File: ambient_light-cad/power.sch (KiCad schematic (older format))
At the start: 27 parts

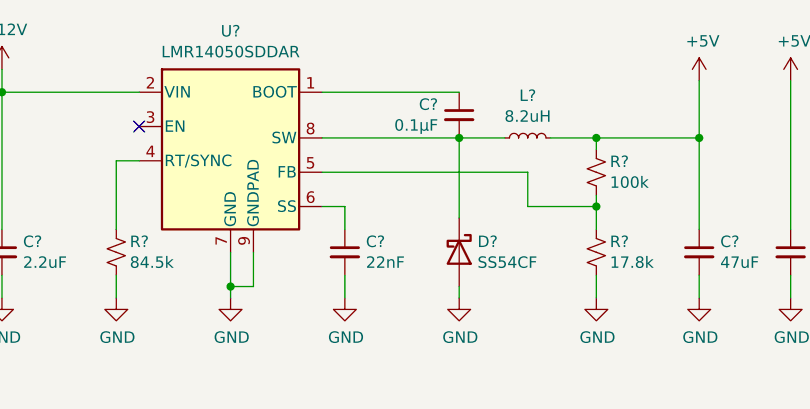
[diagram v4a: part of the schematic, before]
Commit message: [Updated] Symbol field for PCB layout
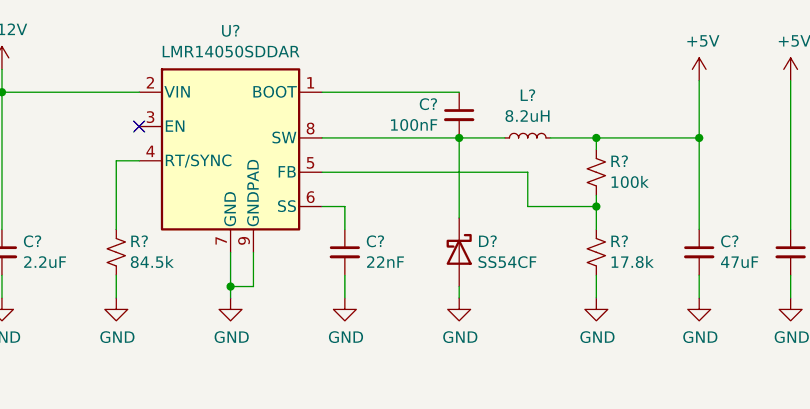
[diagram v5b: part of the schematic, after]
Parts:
- C? (x4): footprint (none) -> Capacitor_SMD:C_0603_1608Metric_Pad1.08x0.95mm_HandSolder
- C? (x4): footprint (none) -> Capacitor_Tantalum_SMD:CP_EIA-3216-18_Kemet-A_Pad1.58x1.35mm_HandSolder
- C?: value 0.1μF -> 100nF; footprint (none) -> Capacitor_SMD:C_0603_1608Metric_Pad1.08x0.95mm_HandSolder
- D?: footprint (none) -> Diode_SMD:D_SMC
- J?: footprint (none) -> Connector_BarrelJack:BarrelJack_Horizontal
- L?: footprint (none) -> Inductor_SMD:L_12x12mm_H8mm
- Q?: footprint (none) -> Package_TO_SOT_SMD:SOT-23
- R? (x5): footprint (none) -> Resistor_SMD:R_0603_1608Metric_Pad0.98x0.95mm_HandSolder
- TP? (x6): footprint (none) -> TestPoint:TestPoint_Pad_D2.0mm
- U?: footprint Package_SO:TI_SO-PowerPAD-8_ThermalVias -> Package_SO:TI_SO-PowerPAD-8
- U? (x2): footprint (none) -> Package_SO:SOIC-8_3.9x4.9mm_P1.27mm
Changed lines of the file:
@@
 F 0 "J?" H 1407 2217 50  0000 C CNN
 F 1 "Barrel_Jack_Switch" H 1407 2126 50  0000 C CNN
-F 2 "" H 1400 1860 50  0001 C CNN
+F 2 "Connector_BarrelJack:BarrelJack_Horizontal" H 1400 1860 50  0001 C CNN
 F 3 "~" H 1400 1860 50  0001 C CNN
 	1    1350 1900
@@
 F 0 "C?" H 3642 2246 50  0000 L CNN
 F 1 "2.2uF" H 3642 2155 50  0000 L CNN
-F 2 "" H 3550 2200 50  0001 C CNN
+F 2 "Capacitor_SMD:C_0603_1608Metric_Pad1.08x0.95mm_HandSolder" H 3550 2200 50  0001 C CNN
 F 3 "~" H 3550 2200 50  0001 C CNN
 	1    3550 2200
@@
 F 0 "R?" H 4109 2246 50  0000 L CNN
 F 1 "84.5k" H 4109 2155 50  0000 L CNN
-F 2 "" H 4050 2200 50  0001 C CNN
+F 2 "Resistor_SMD:R_0603_1608Metric_Pad0.98x0.95mm_HandSolder" H 4050 2200 50  0001 C CNN
 F 3 "~" H 4050 2200 50  0001 C CNN
 	1    4050 2200
@@
 F 0 "L?" V 6035 1700 50  0000 C CNN
 F 1 "8.2uH" V 5944 1700 50  0000 C CNN
-F 2 "" H 5850 1700 50  0001 C CNN
+F 2 "Inductor_SMD:L_12x12mm_H8mm" H 5850 1700 50  0001 C CNN
 F 3 "~" H 5850 1700 50  0001 C CNN
 	1    5850 1700
@@
 F 0 "C?" H 6692 2246 50  0000 L CNN
 F 1 "47uF" H 6692 2155 50  0000 L CNN
-F 2 "" H 6600 2200 50  0001 C CNN
+F 2 "Capacitor_Tantalum_SMD:CP_EIA-3216-18_Kemet-A_Pad1.58x1.35mm_HandSolder" H 6600 2200 50  0001 C CNN
 F 3 "~" H 6600 2200 50  0001 C CNN
 	1    6600 2200
@@
 F 0 "R?" H 6209 2246 50  0000 L CNN
 F 1 "17.8k" H 6209 2155 50  0000 L CNN
-F 2 "" H 6150 2200 50  0001 C CNN
+F 2 "Resistor_SMD:R_0603_1608Metric_Pad0.98x0.95mm_HandSolder" H 6150 2200 50  0001 C CNN
 F 3 "~" H 6150 2200 50  0001 C CNN
 	1    6150 2200
@@
 F 0 "R?" H 6209 1896 50  0000 L CNN
 F 1 "100k" H 6209 1805 50  0000 L CNN
-F 2 "" H 6150 1850 50  0001 C CNN
+F 2 "Resistor_SMD:R_0603_1608Metric_Pad0.98x0.95mm_HandSolder" H 6150 1850 50  0001 C CNN
 F 3 "~" H 6150 1850 50  0001 C CNN
 	1    6150 1850
@@
 P 5550 1600
 F 0 "C?" H 5642 1646 50  0000 L CNN
-F 1 "0.1μF" H 5642 1555 50  0000 L CNN
-F 2 "" H 5550 1600 50  0001 C CNN
+F 1 "100nF" H 5642 1555 50  0000 L CNN
+F 2 "Capacitor_SMD:C_0603_1608Metric_Pad1.08x0.95mm_HandSolder" H 5550 1600 50  0001 C CNN
 F 3 "~" H 5550 1600 50  0001 C CNN
 	1    5550 1600
@@
 F 0 "D?" V 5504 2280 50  0000 L CNN
 F 1 "SS54CF" V 5595 2280 50  0000 L CNN
-F 2 "" H 5550 2200 50  0001 C CNN
+F 2 "Diode_SMD:D_SMC" H 5550 2200 50  0001 C CNN
 F 3 "~" H 5550 2200 50  0001 C CNN
 	1    5550 2200
@@
 F 0 "C?" H 5142 2246 50  0000 L CNN
 F 1 "22nF" H 5142 2155 50  0000 L CNN
-F 2 "" H 5050 2200 50  0001 C CNN
+F 2 "Capacitor_SMD:C_0603_1608Metric_Pad1.08x0.95mm_HandSolder" H 5050 2200 50  0001 C CNN
 F 3 "~" H 5050 2200 50  0001 C CNN
 	1    5050 2200
@@
 F 0 "U?" H 4550 2167 50  0000 C CNN
 F 1 "LMR14050SDDAR" H 4550 2076 50  0000 C CNN
-F 2 "Package_SO:TI_SO-PowerPAD-8_ThermalVias" H 4600 1250 50  0001 L CIN
+F 2 "Package_SO:TI_SO-PowerPAD-8" H 4600 1250 50  0001 L CIN
 F 3 "http://www.ti.com/lit/ds/symlink/tps54360.pdf" H 4550 1700 50  0001 C CNN
 	1    4550 1700
@@
 F 0 "C?" H 7092 2246 50  0000 L CNN
 F 1 "47uF" H 7092 2155 50  0000 L CNN
-F 2 "" H 7000 2200 50  0001 C CNN
+F 2 "Capacitor_Tantalum_SMD:CP_EIA-3216-18_Kemet-A_Pad1.58x1.35mm_HandSolder" H 7000 2200 50  0001 C CNN
 F 3 "~" H 7000 2200 50  0001 C CNN
 	1    7000 2200
@@
 F 0 "C?" H 7492 2246 50  0000 L CNN
 F 1 "47uF" H 7492 2155 50  0000 L CNN
-F 2 "" H 7400 2200 50  0001 C CNN
+F 2 "Capacitor_Tantalum_SMD:CP_EIA-3216-18_Kemet-A_Pad1.58x1.35mm_HandSolder" H 7400 2200 50  0001 C CNN
 F 3 "~" H 7400 2200 50  0001 C CNN
 	1    7400 2200
@@
 F 0 "C?" H 7892 2246 50  0000 L CNN
 F 1 "47uF" H 7892 2155 50  0000 L CNN
-F 2 "" H 7800 2200 50  0001 C CNN
+F 2 "Capacitor_Tantalum_SMD:CP_EIA-3216-18_Kemet-A_Pad1.58x1.35mm_HandSolder" H 7800 2200 50  0001 C CNN
 F 3 "~" H 7800 2200 50  0001 C CNN
 	1    7800 2200
@@
 F 0 "C?" H 3242 2246 50  0000 L CNN
 F 1 "2.2uF" H 3242 2155 50  0000 L CNN
-F 2 "" H 3150 2200 50  0001 C CNN
+F 2 "Capacitor_SMD:C_0603_1608Metric_Pad1.08x0.95mm_HandSolder" H 3150 2200 50  0001 C CNN
 F 3 "~" H 3150 2200 50  0001 C CNN
 	1    3150 2200
@@
 F 0 "C?" H 2842 2246 50  0000 L CNN
 F 1 "100nF" H 2842 2155 50  0000 L CNN
-F 2 "" H 2750 2200 50  0001 C CNN
+F 2 "Capacitor_SMD:C_0603_1608Metric_Pad1.08x0.95mm_HandSolder" H 2750 2200 50  0001 C CNN
 F 3 "~" H 2750 2200 50  0001 C CNN
 	1    2750 2200
@@
 F 0 "Q?" V 3699 4900 50  0000 C CNN
 F 1 "Q_PMOS_GSD" V 3790 4900 50  0000 C CNN
-F 2 "" H 3650 5000 50  0001 C CNN
+F 2 "Package_TO_SOT_SMD:SOT-23" H 3650 5000 50  0001 C CNN
 F 3 "~" H 3450 4900 50  0001 C CNN
 	1    3450 4900
@@
 F 0 "U?" H 3050 4517 50  0000 C CNN
 F 1 "LM2904" H 3050 4426 50  0000 C CNN
-F 2 "" H 3050 4150 50  0001 C CNN
+F 2 "Package_SO:SOIC-8_3.9x4.9mm_P1.27mm" H 3050 4150 50  0001 C CNN
 F 3 "http://www.ti.com/lit/ds/symlink/lm358.pdf" H 3050 4150 50  0001 C CNN
 	1    3050 4150
@@
 F 0 "U?" H 1258 3946 50  0000 L CNN
 F 1 "LM2904" H 1258 3855 50  0000 L CNN
-F 2 "" H 1300 3900 50  0001 C CNN
+F 2 "Package_SO:SOIC-8_3.9x4.9mm_P1.27mm" H 1300 3900 50  0001 C CNN
 F 3 "http://www.ti.com/lit/ds/symlink/lm358.pdf" H 1300 3900 50  0001 C CNN
 	3    1300 3900
@@
 F 0 "R?" H 1818 3696 50  0000 L CNN
 F 1 "10k" H 1818 3605 50  0000 L CNN
-F 2 "" H 1750 3650 50  0001 C CNN
+F 2 "Resistor_SMD:R_0603_1608Metric_Pad0.98x0.95mm_HandSolder" H 1750 3650 50  0001 C CNN
 F 3 "~" H 1750 3650 50  0001 C CNN
 	1    1750 3650
@@
 F 0 "R?" H 1818 4196 50  0000 L CNN
 F 1 "10k" H 1818 4105 50  0000 L CNN
-F 2 "" H 1750 4150 50  0001 C CNN
+F 2 "Resistor_SMD:R_0603_1608Metric_Pad0.98x0.95mm_HandSolder" H 1750 4150 50  0001 C CNN
 F 3 "~" H 1750 4150 50  0001 C CNN
 	1    1750 4150
@@
 F 0 "TP?" H 2508 3918 50  0000 L CNN
 F 1 "TP_OP+" H 2508 3827 50  0000 L CNN
-F 2 "" H 2650 3800 50  0001 C CNN
+F 2 "TestPoint:TestPoint_Pad_D2.0mm" H 2650 3800 50  0001 C CNN
 F 3 "~" H 2650 3800 50  0001 C CNN
 	1    2450 3800
@@
 F 0 "TP?" H 2392 4426 50  0000 R CNN
 F 1 "TP_OP-" H 2392 4517 50  0000 R CNN
-F 2 "" H 2650 4400 50  0001 C CNN
+F 2 "TestPoint:TestPoint_Pad_D2.0mm" H 2650 4400 50  0001 C CNN
 F 3 "~" H 2650 4400 50  0001 C CNN
 	1    2450 4400
@@
 F 0 "TP?" V 3596 4338 50  0000 L CNN
 F 1 "TP_OP_OUT" V 3505 4338 50  0000 L CNN
-F 2 "" H 3750 4150 50  0001 C CNN
+F 2 "TestPoint:TestPoint_Pad_D2.0mm" H 3750 4150 50  0001 C CNN
 F 3 "~" H 3750 4150 50  0001 C CNN
 	1    3550 4150
@@
 F 0 "TP?" V 2700 5250 50  0000 C CNN
 F 1 "TP_VBUS" V 2600 5350 50  0000 C CNN
-F 2 "" H 2850 5000 50  0001 C CNN
+F 2 "TestPoint:TestPoint_Pad_D2.0mm" H 2850 5000 50  0001 C CNN
 F 3 "~" H 2850 5000 50  0001 C CNN
 	1    2650 5000
@@
 F 0 "TP?" V 1904 1688 50  0000 L CNN
 F 1 "TP_12V" V 1995 1688 50  0000 L CNN
-F 2 "" H 2150 1500 50  0001 C CNN
+F 2 "TestPoint:TestPoint_Pad_D2.0mm" H 2150 1500 50  0001 C CNN
 F 3 "~" H 2150 1500 50  0001 C CNN
 	1    1950 1500
@@
 F 0 "TP?" V 4204 5188 50  0000 L CNN
 F 1 "TP_VCC" V 4295 5188 50  0000 L CNN
-F 2 "" H 4450 5000 50  0001 C CNN
+F 2 "TestPoint:TestPoint_Pad_D2.0mm" H 4450 5000 50  0001 C CNN
 F 3 "~" H 4450 5000 50  0001 C CNN
 	1    4250 5000

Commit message: [Modified] sync file
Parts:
- U?: symbol ambient_light-cad:LMR14050SDDAR -> ambient_light-cad-rescue:LMR14050SDDAR-ambient_light-cad
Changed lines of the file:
@@
 $Descr A4 11693 8268
 encoding utf-8
-Sheet 2 2
+Sheet 4 4
 Title ""
 Date ""
@@
 $EndComp
 $Comp
-L ambient_light-cad:LMR14050SDDAR U?
+L ambient_light-cad-rescue:LMR14050SDDAR-ambient_light-cad U?
 U 1 1 5FDC2F39
 P 4550 1700
